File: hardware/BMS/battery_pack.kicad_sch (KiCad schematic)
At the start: 20 parts, among them Q1 PMOS, Q2 PMOS, Q3 AOSP36326C, Q4 AOSP36326C, U3 MM3220AA2NRH

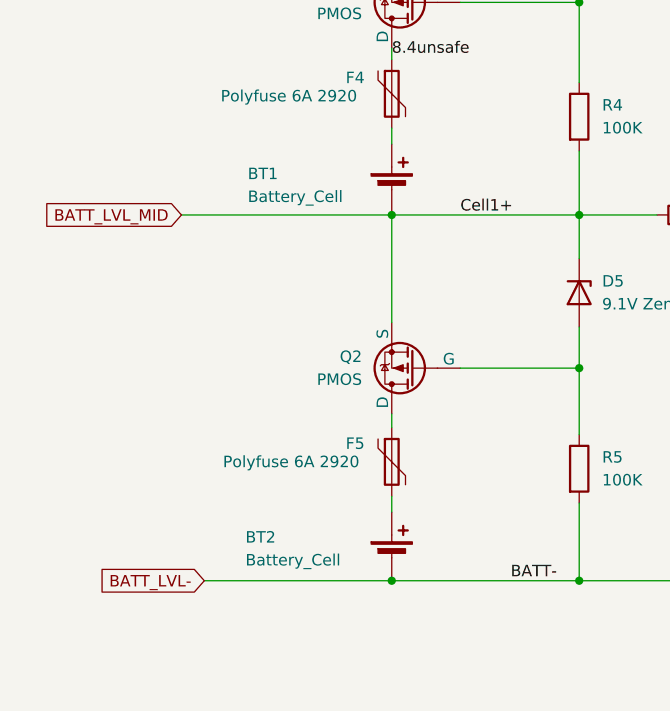
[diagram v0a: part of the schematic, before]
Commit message: Hardware - Controller - Rev 0.3
* Consolidate various asset dirs into single symlinked directory.
* Fixes major flaw with previous atmega328 layout - wrong schematic symbol caused incorrect routing
* Use smaller crystal closer to mcu
* Add QR to silkscreen
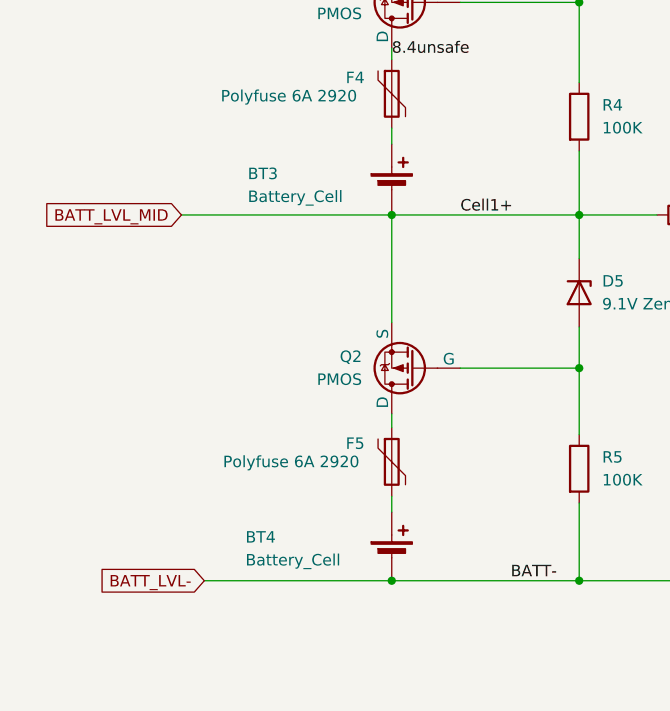
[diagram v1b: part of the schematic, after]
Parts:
- renumbered BT1 to BT3, BT2 to BT4
